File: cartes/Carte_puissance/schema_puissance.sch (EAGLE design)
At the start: 25 parts, among them X1 MICROMATCH-8, X2 GMSTBA2

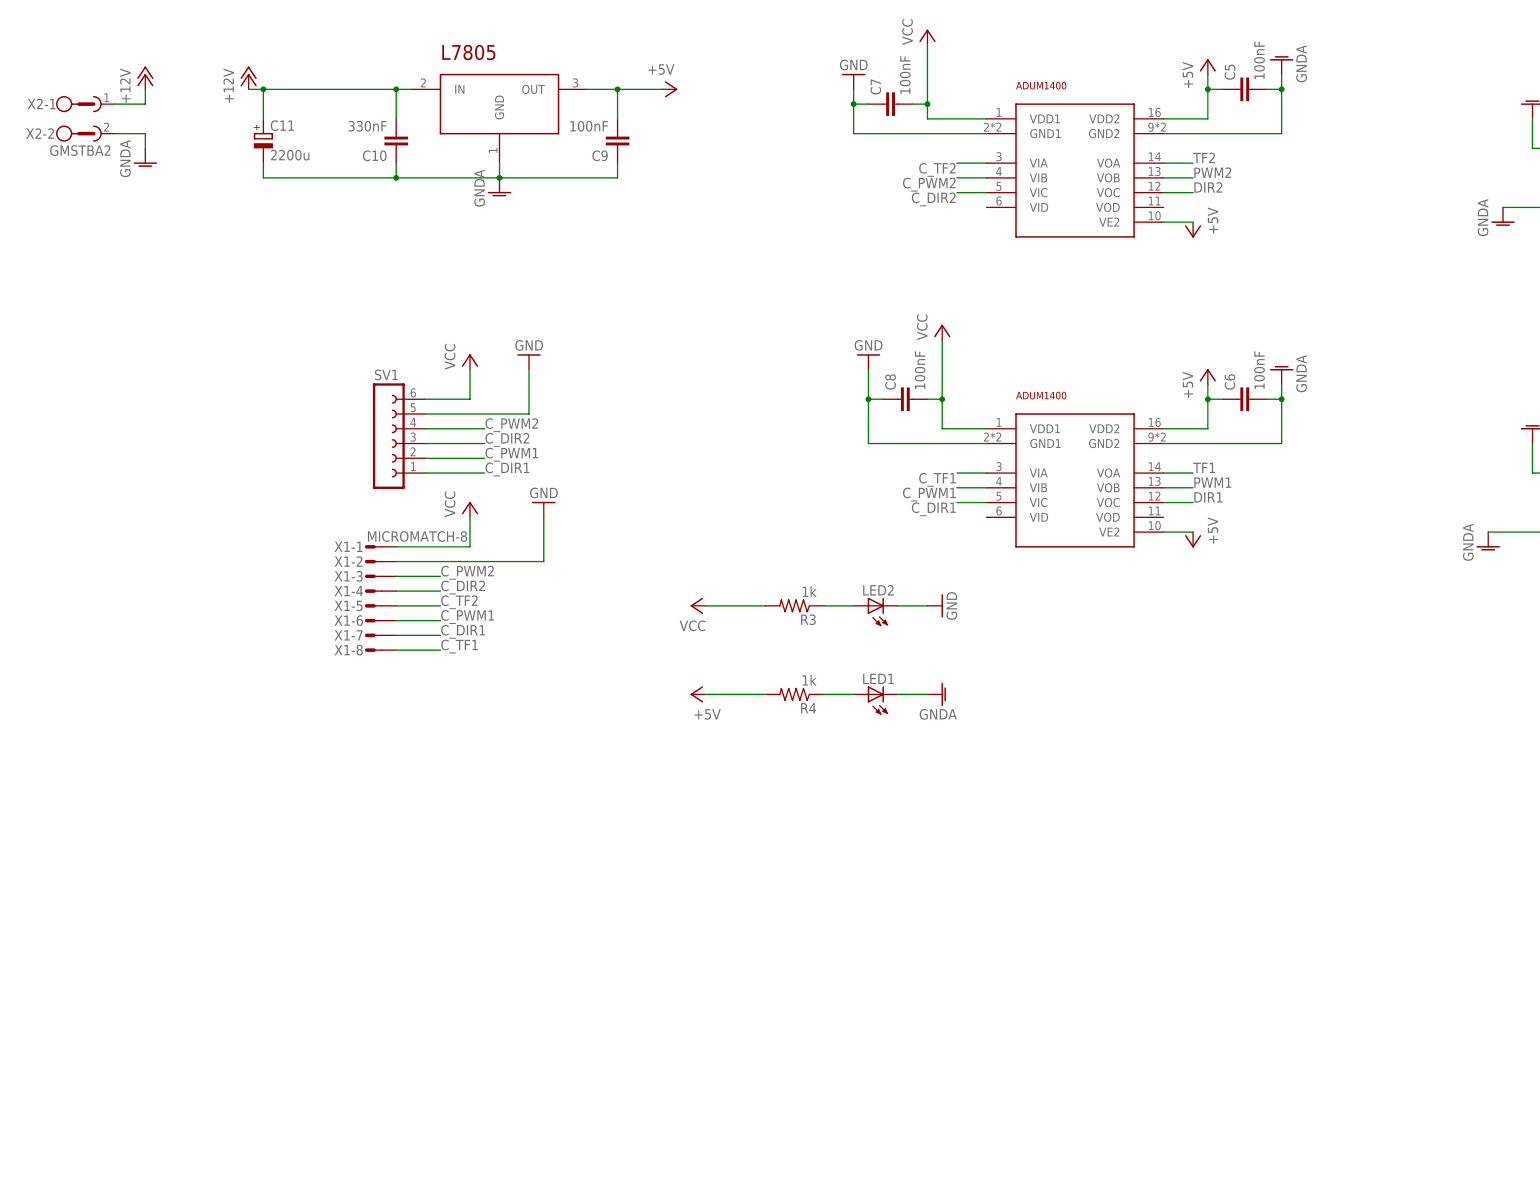
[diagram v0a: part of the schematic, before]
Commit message: Ajout carte puissance
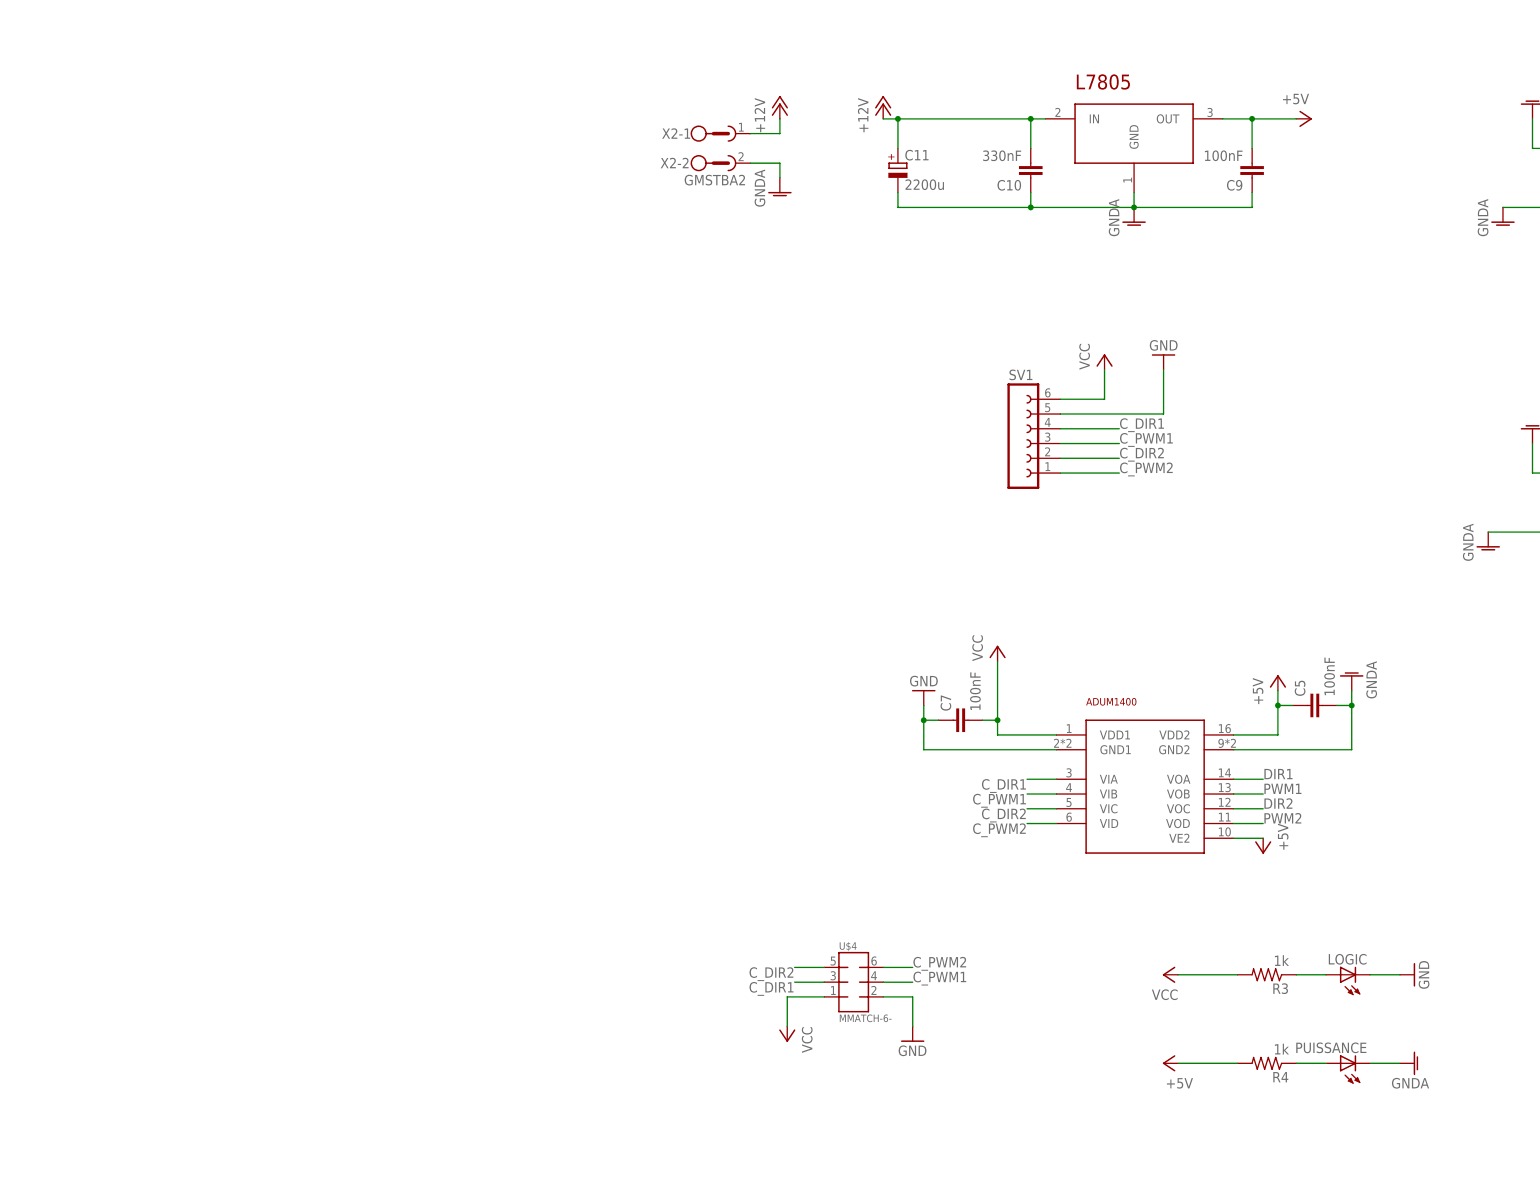
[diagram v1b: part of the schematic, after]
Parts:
- removed C6, C8: 100nF, rcl:C-EUC0805
- removed LED1, LED2: (no value), led:LEDSML0805
- removed X1: MICROMATCH-8, con-amp-micromatch:MICROMATCH-8
- added LOGIC, PUISSANCE: (no value), led:LEDSML0805
- U$4: value ADUM1400S -> MMATCH-6-; device analog-devices:ADUM1400S -> jt-con-micromatch:MMATCH-6-
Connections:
- removed net C_TF1: U$4.VIA, X1-8.S
- removed net C_TF2: U$3.VIA, X1-5.S
- net +5V: no longer C6.1, U$4.VDD2, U$4.VE2
- net C_DIR1: now also SV1.4, U$3.VIA, U$4.5; no longer SV1.1, U$4.VIC, X1-7.S
- net C_DIR2: now also SV1.2, U$4.7; no longer SV1.3, X1-4.S
- net C_PWM1: now also SV1.3, U$3.VIB, U$4.6; no longer SV1.2, U$4.VIB, X1-6.S
- net C_PWM2: now also SV1.1, U$3.VID, U$4.8; no longer SV1.4, U$3.VIB, X1-3.S
- net DIR1: now also U$3.VOA; no longer U$4.VOC
- net GND: now also LOGIC.C, U$4.4; no longer C8.1, LED2.C, U$4.GND1, X1-2.S
- net GNDA: now also PUISSANCE.C; no longer C6.2, LED1.C, U$4.GND2
- net N$2: now also PUISSANCE.A; no longer LED1.A
- net N$4: now also LOGIC.A; no longer LED2.A
- net PWM1: now also U$3.VOB; no longer U$4.VOB
- net PWM2: now also U$3.VOD; no longer U$3.VOB
- net TF1: no longer U$4.VOA
- net TF2: no longer U$3.VOA
- net VCC: now also U$4.3; no longer C8.2, U$4.VDD1, X1-1.S
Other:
- moved on the sheet: C10, C11, C5, C7, C9, R3, R4, SV1, X2-1, X2-2
